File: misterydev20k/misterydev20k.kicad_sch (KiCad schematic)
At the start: 45 parts, among them J1 SWD, J2 USB_C_Receptacle_USB2.0, SW1 SW_Push, U1 XC6206PxxxMR-Regulator_Linear, U2 W25Q128JVS, U3 USBLC6-2SC6, U4 RP2040, Y1 12MHz

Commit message: Some dev board progress
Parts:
- added R51: 22, Resistor_SMD:R_0402_1005Metric, symbol Device:R_Small
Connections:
- net TCK: now also R51.2; no longer U4.18 (GPIO15)
- net ~{CFG}: now reaches U4.32 (GPIO21)
- net MODE0: now reaches U4.35 (GPIO23)
- net MODE1: now reaches U4.36 (GPIO24)
- new net: R51.1, U4.18 (GPIO15)
- no-connect marks 10 -> 7
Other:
- sheet GW2AR-LV18 FPGA ports: added MODE[0..1], ~{CFG}; removed none
- moved on the sheet: D1, R9

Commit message: More updates in dev20k
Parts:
- removed C4: 1uF, Capacitor_SMD:C_0402_1005Metric, symbol Device:C_Small
- removed FB5: MPZ1608S101, Inductor_SMD:L_0603_1608Metric, symbol Device:FerriteBead
- removed JP1: 3.3V, Jumper:SolderJumper-3_P1.3mm_Bridged12_RoundedPad1.0x1.5mm, symbol Jumper:SolderJumper_3_Bridged12
- removed R8: 1k, Resistor_SMD:R_0402_1005Metric, symbol Device:R_Small
- removed U1: XC6206PxxxMR-Regulator_Linear, Package_TO_SOT_SMD:SOT-23, symbol kicad-keyboard-parts:XC6206PxxxMR-Regulator_Linear
- added C37: 100nF, Capacitor_SMD:C_0402_1005Metric, symbol Device:C_Small
- added C38: 10uF, Capacitor_SMD:C_0402_1005Metric, symbol Device:C_Small
- added FB1: MPZ1608S101, Inductor_SMD:L_0603_1608Metric, symbol Device:FerriteBead
- added L1: 2.2uH, Inductor_SMD:L_0805_2012Metric, symbol Device:L
- added R36: 68k, Resistor_SMD:R_0402_1005Metric, symbol Device:R_Small
- added R37: 15k, Resistor_SMD:R_0402_1005Metric, symbol Device:R_Small
- added U10: TLV62569DBV, Package_TO_SOT_SMD:SOT-23-5, symbol Regulator_Switching:TLV62569DBV
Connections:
- net +3V3: now also FB1.2
- net +5V: now also C37.2, U10.1 (EN), U10.4 (VIN)
- net GND: now also C37.1, C38.1, R37.2, U10.2 (GND)
- new net: C38.2, FB1.1, L1.2, R36.1
- new net: R36.2, R37.1, U10.5 (FB)
- new net: L1.1, U10.3 (SW)
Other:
- sheet GW2AR-LV18 FPGA ports: added +3.3V; removed VCC33
- sheet USB Hub ports: added none; removed 12MHz
- note added: "or MT3520B"
- note removed: "RP2040 main 3.3V linear regulated power supply. Optionally replaced by the FPGAs switch mode 3.3V supply."
- moved on the sheet: C11, C12, C13, C14, C6, C7, C8

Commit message: dev20k update
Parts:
- removed C37: 100nF, Capacitor_SMD:C_0402_1005Metric, symbol Device:C_Small
- removed C38: 10uF, Capacitor_SMD:C_0402_1005Metric, symbol Device:C_Small
- removed FB1: MPZ1608S101, Inductor_SMD:L_0603_1608Metric, symbol Device:FerriteBead
- removed L1: 2.2uH, Inductor_SMD:L_0805_2012Metric, symbol Device:L
- removed R36: 68k, Resistor_SMD:R_0402_1005Metric, symbol Device:R_Small
- removed R37: 15k, Resistor_SMD:R_0402_1005Metric, symbol Device:R_Small
- removed U10: TLV62569DBV, Package_TO_SOT_SMD:SOT-23-5, symbol Regulator_Switching:TLV62569DBV
- added C51, C54: 100nF, Capacitor_SMD:C_0402_1005Metric, symbol Device:C_Small
- added C52, C57: 100nF, Capacitor_SMD:C_0603_1608Metric, symbol Device:C_Small
- added C53: 10uF, Capacitor_SMD:C_0603_1608Metric, symbol Device:C_Small
- added C55: 22pF, Capacitor_SMD:C_0402_1005Metric, symbol Device:C_Small
- added C56: 22uF, Capacitor_SMD:C_0603_1608Metric, symbol Device:C_Small
- added L3: 3.3uH, Inductor_SMD:L_Sunlord_MWSA0402S, symbol Device:L
- added R53: 47k, Resistor_SMD:R_0402_1005Metric, symbol Device:R_Small
- added R54, R55: 30k 1%, Resistor_SMD:R_0402_1005Metric, symbol Device:R_Small
- added R8: 30k, Resistor_SMD:R_0402_1005Metric, symbol Device:R_Small
- added U1: SY8113BADC, Package_TO_SOT_SMD:TSOT-23-6, symbol Regulator_Switching:LM2842Y
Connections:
- net +3V3: now also C55.2, C56.1, C57.1, L3.2, R54.2
- net +5V: now also C52.1, C53.1, R53.2, U1.5 (VIN)
- net GND: now also C51.1, C52.2, C53.2, C56.2, C57.2, R55.1, R8.1, U1.2 (GND)
- net ~{SD_DET}: now reaches U4.9 (GPIO7)
- net SD_CLK renamed SD_CLK_PI
- new net: C55.1, R54.1, R55.2, U1.3 (FB)
- new net: C54.1, U1.1 (BOOST)
- new net: C54.2, L3.1, U1.6 (SW)
- new net: C51.2, R53.1, R8.2, U1.4 (EN)
- no-connect marks 7 -> 6
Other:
- sheet GW2AR-LV18 FPGA ports: added SD_CLK_PI, ~{SD_DET}; removed SD_CLK
- note added: "TODO: Check Inductor!!!"
- note removed: "or MT3520B"

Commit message: Another board update
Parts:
- R54: value 30k 1% -> 15k 1%
- R55: value 30k 1% -> 3k3 1%
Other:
- note removed: "TODO: Check Inductor!!!"
- moved on the sheet: C55, C56, C57, L3, R54, R55

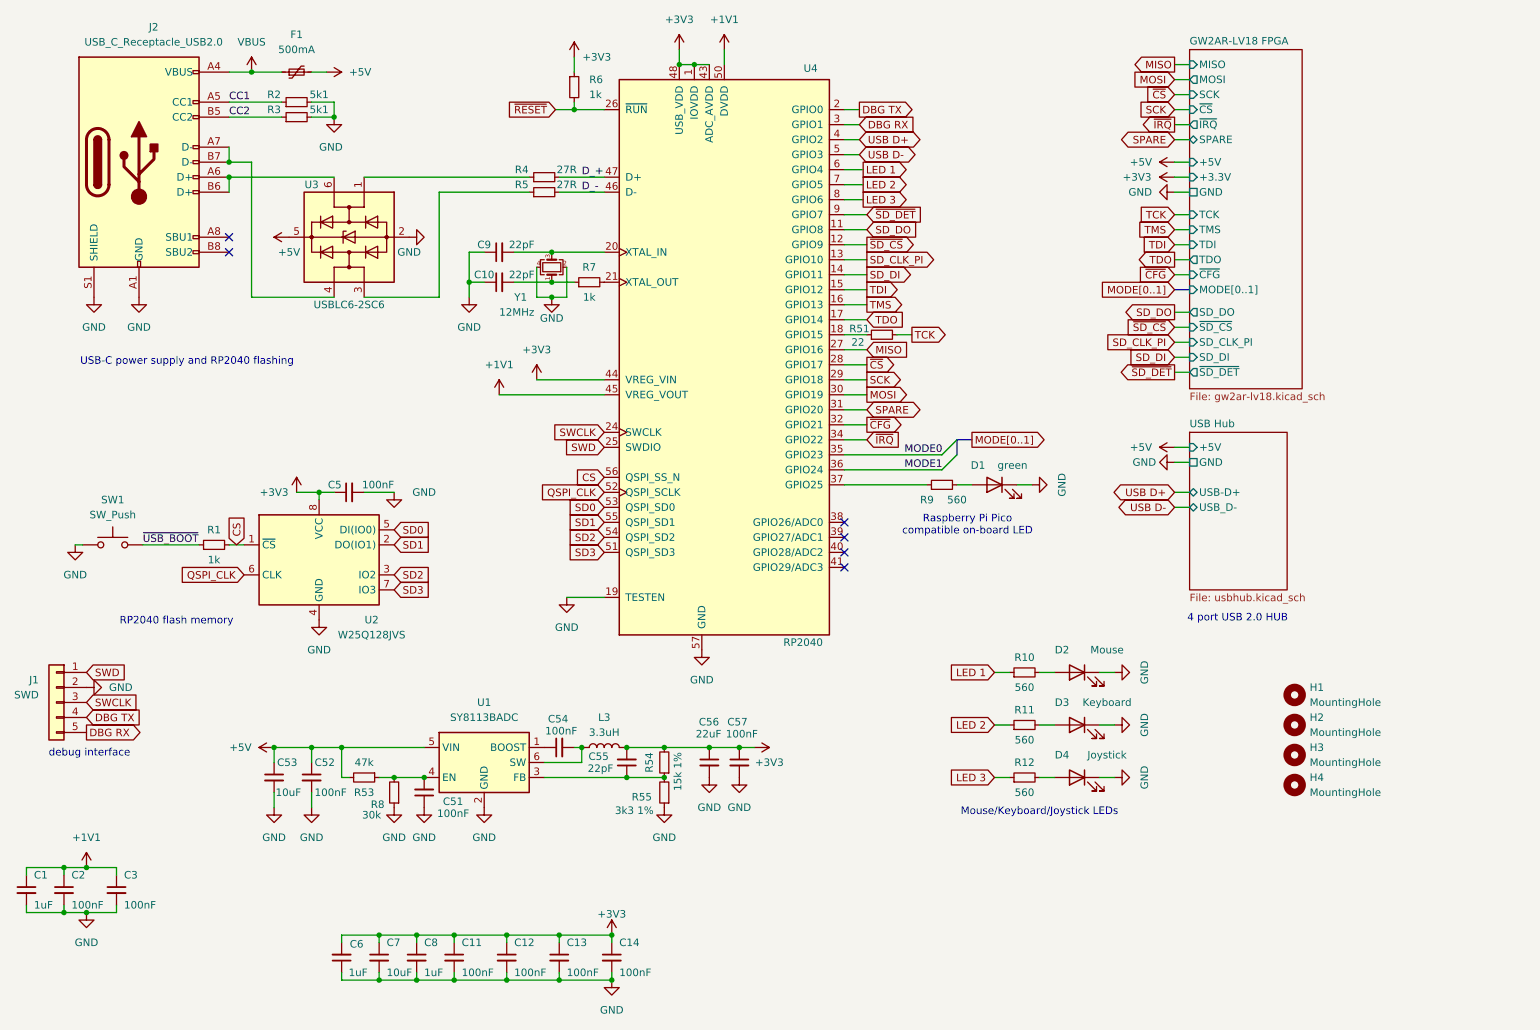
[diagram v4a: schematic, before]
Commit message: Fix dev20k schematic
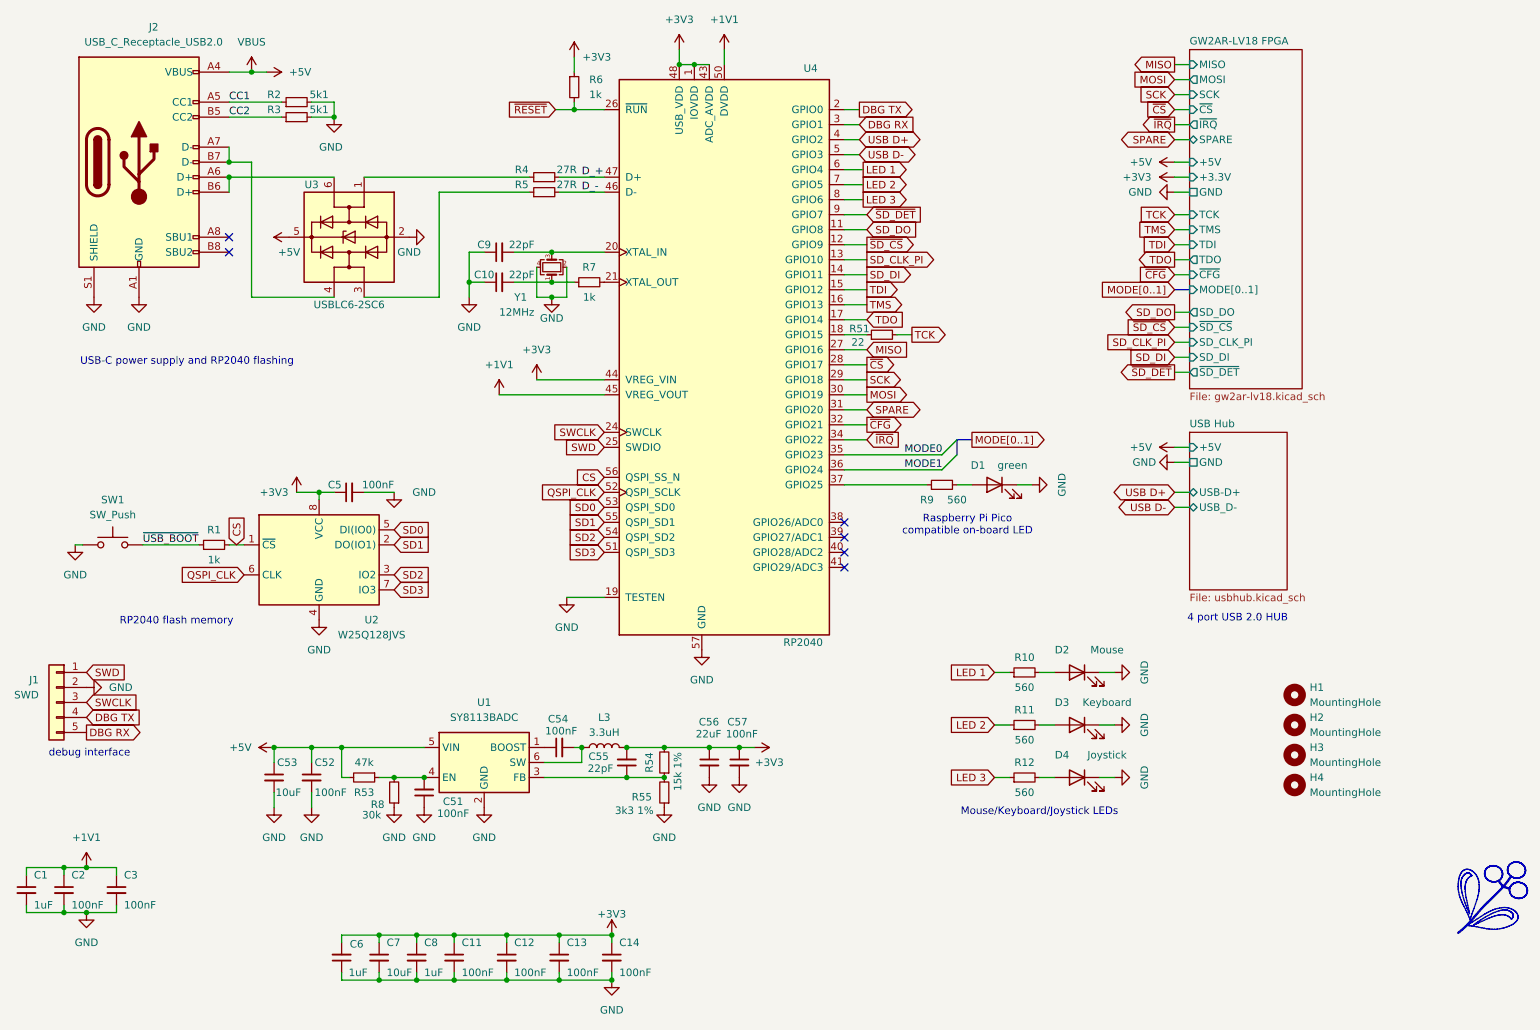
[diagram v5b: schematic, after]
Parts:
- removed F1: 500mA, Fuse:Fuse_1206_3216Metric, symbol Device:Polyfuse_Small
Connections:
- net VBUS is gone; now on net +5V: J2.A4 (VBUS), J2.A9 (VBUS), J2.B4 (VBUS), J2.B9 (VBUS)
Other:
- title: MiSTery 20k Development Board -> MiSTeryDev 20k - FPGA Companion MCU

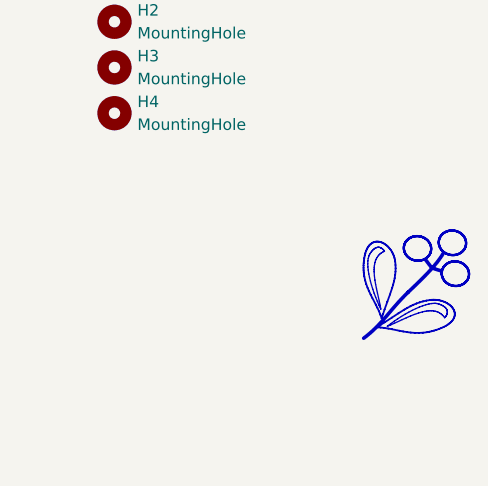
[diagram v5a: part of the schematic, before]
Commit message: Update pin table
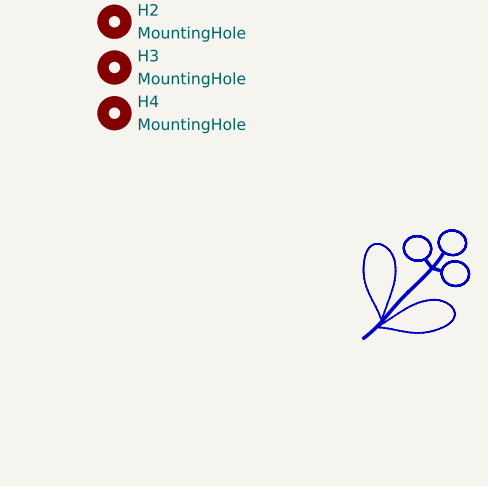
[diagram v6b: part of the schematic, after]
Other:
- title: MiSTeryDev 20k - FPGA Companion MCU -> MiSTle - MiSTeryDev20k
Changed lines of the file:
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@@
 	(paper "A4")
 	(title_block
-		(title "MiSTeryDev 20k - FPGA Companion MCU")
+		(title "MiSTle - MiSTeryDev20k")
 		(date "2025-08-28")
 		(rev "1.0")
 		(company "Till Harbaum")
-	)
-	(polyline
-		(pts
-			(xy 279.5138 176.0698) (xy 279.6412 176.0823) (xy 279.7608 176.1043) (xy 279.8723 176.1363) (xy 279.9762 176.174)
-			(xy 280.0733 176.2131) (xy 280.164 176.2535) (xy 280.2482 176.2952) (xy 280.3261 176.3381) (xy 280.3978 176.3821)
-			(xy 280.4635 176.4271) (xy 280.5234 176.4731) (xy 280.5774 176.52) (xy 280.6258 176.5676) (xy 280.6687 176.616)
-			(xy 280.7062 176.6651) (xy 280.7384 176.7148) (xy 280.7655 176.7649) (xy 280.7877 176.8155) (xy 280.8049 176.8664)
-			(xy 280.8175 176.9177) (xy 280.8254 176.9691) (xy 280.8289 177.0206) (xy 280.828 177.0722) (xy 280.8229 177.1238)
-			(xy 280.8137 177.1753) (xy 280.8006 177.2266) (xy 280.7836 177.2777) (xy 280.763 177.3284) (xy 280.7388 177.3787)
-			(xy 280.7112 177.4286) (xy 280.6802 177.4779) (xy 280.6461 177.5266) (xy 280.609 177.5746) (xy 280.5689 177.6218)
-			(xy 280.5261 177.6682) (xy 280.4018 177.5021) (xy 280.2674 177.3583) (xy 280.1235 177.2358) (xy 279.9705 177.1336)
-			(xy 279.8089 177.0507) (xy 279.6394 176.9862) (xy 279.4624 176.9392) (xy 279.2784 176.9086) (xy 279.0881 176.8935)
-			(xy 278.8919 176.8929) (xy 278.6903 176.906) (xy 278.4838 176.9317) (xy 278.2731 176.969) (xy 278.0586 177.017)
-			(xy 277.6204 177.1414) (xy 277.1734 177.2971) (xy 276.7219 177.4764) (xy 276.2701 177.6716) (xy 275.8221 177.8751)
-			(xy 274.9549 178.276) (xy 274.544 178.4582) (xy 274.1539 178.6178) (xy 274.5308 178.3322) (xy 274.9192 178.0535)
-			(xy 275.3163 177.784) (xy 275.719 177.5259) (xy 276.1241 177.2814) (xy 276.5287 177.0529) (xy 276.9297 176.8425)
-			(xy 277.324 176.6525) (xy 277.7086 176.4851) (xy 278.0805 176.3427) (xy 278.4365 176.2274) (xy 278.7736 176.1414)
-			(xy 279.0888 176.0871) (xy 279.379 176.0666) (xy 279.5138 176.0698)
-		)
-		(stroke
-			(width -0.0001)
-			(type solid)
-		)
-		(fill
-			(type color)
-			(color 30 188 94 1)
-		)
+		(comment 1 "FPGA Companion MCU")
 	)
 	(bezier
@@
 			(width 0.4)
 			(type solid)
+			(color 0 0 0 1)
 		)
 		(fill
@@
 		)
 	)
-	(polyline
-		(pts
-			(xy 273.2247 169.8384) (xy 273.2758 169.8459) (xy 273.3261 169.8576) (xy 273.3754 169.8734) (xy 273.4238 169.8932)
-			(xy 273.4712 169.9169) (xy 273.5176 169.9442) (xy 273.5628 169.975) (xy 273.607 170.0093) (xy 273.6499 170.0468)
-			(xy 273.6916 170.0874) (xy 273.732 170.131) (xy 273.7711 170.1774) (xy 273.8089 170.2265) (xy 273.8452 170.2781)
-			(xy 273.6567 170.3647) (xy 273.4879 170.4658) (xy 273.3378 170.5808) (xy 273.2057 170.7089) (xy 273.0907 170.8494)
-			(xy 272.992 171.0015) (xy 272.9088 171.1647) (xy 272.8402 171.3381) (xy 272.7854 171.521) (xy 272.7436 171.7127)
-			(xy 272.714 171.9126) (xy 272.6957 172.1198) (xy 272.6879 172.3337) (xy 272.6897 172.5535) (xy 272.7192 173.008)
-			(xy 272.7774 173.4778) (xy 272.8577 173.9569) (xy 272.9535 174.4397) (xy 273.0583 174.9204) (xy 273.2679 175.8525)
-			(xy 273.3596 176.2925) (xy 273.4336 176.7075) (xy 273.2336 176.279) (xy 273.0428 175.8406) (xy 272.8628 175.3957)
-			(xy 272.6952 174.9478) (xy 272.5414 174.5003) (xy 272.403 174.0567) (xy 272.2817 173.6204) (xy 272.1789 173.1949)
-			(xy 272.0961 172.7837) (xy 272.0351 172.3903) (xy 271.9972 172.018) (xy 271.984 171.6703) (xy 271.9972 171.3507)
-			(xy 272.0382 171.0627) (xy 272.1087 170.8097) (xy 272.1554 170.6974) (xy 272.21 170.5951) (xy 272.2687 170.5015)
-			(xy 272.3274 170.4147) (xy 272.386 170.3346) (xy 272.4445 170.2611) (xy 272.5028 170.1939) (xy 272.5609 170.133)
-			(xy 272.6187 170.0782) (xy 272.6763 170.0294) (xy 272.7335 169.9865) (xy 272.7902 169.9492) (xy 272.8466 169.9174)
-			(xy 272.9024 169.8911) (xy 272.9578 169.87) (xy 273.0125 169.854) (xy 273.0666 169.843) (xy 273.12 169.8369)
-			(xy 273.1727 169.8354) (xy 273.2247 169.8384)
-		)
-		(stroke
-			(width -0.0001)
-			(type solid)
-		)
-		(fill
-			(type color)
-			(color 30 188 94 1)
-		)
-	)
 	(bezier
 		(pts
@@
 			(width 0.4)
 			(type solid)
+			(color 0 0 0 1)
 		)
 		(fill
@@
 			(width 0.2)
 			(type solid)
+			(color 0 0 0 1)
 		)
 		(fill
@@
 	(polyline
 		(pts
-			(xy 273.2477 169.2225) (xy 273.3911 169.2549) (xy 273.5339 169.3026) (xy 273.6752 169.365) (xy 273.8142 169.4415)
-			(xy 273.95 169.5313) (xy 274.0819 169.6339) (xy 274.2089 169.7484) (xy 274.3302 169.8744) (xy 274.4451 170.011)
-			(xy 274.5525 170.1577) (xy 274.6518 170.3138) (xy 274.742 170.4786) (xy 274.8223 170.6514) (xy 274.8918 170.8316)
-			(xy 274.9498 171.0185) (xy 274.9954 171.2115) (xy 275.0277 171.4099) (xy 275.0648 171.8037) (xy 275.0758 172.1837)
-			(xy 275.0626 172.5529) (xy 275.027 172.9144) (xy 274.9709 173.2712) (xy 274.8961 173.6262) (xy 274.8044 173.9824)
-			(xy 274.6978 174.3429) (xy 274.4468 175.0887) (xy 274.158 175.8875) (xy 273.8461 176.7634) (xy 273.6861 177.2377)
-			(xy 273.5259 177.7403) (xy 273.3867 177.3352) (xy 273.2277 176.9454) (xy 273.0536 176.5673) (xy 272.8692 176.1971)
-			(xy 272.4888 175.4658) (xy 272.3023 175.0973) (xy 272.1246 174.7221) (xy 271.9605 174.3364) (xy 271.8149 173.9365)
-			(xy 271.6925 173.5187) (xy 271.598 173.0794) (xy 271.5628 172.8506) (xy 271.5364 172.6149) (xy 271.5193 172.3721)
-			(xy 271.5122 172.1215) (xy 271.5157 171.8628) (xy 271.5304 171.5955) (xy 271.5569 171.3191) (xy 271.5957 171.0332)
-			(xy 271.6473 170.7553) (xy 271.7108 170.5027) (xy 271.7855 170.2747) (xy 271.8706 170.0708) (xy 271.9652 169.8903)
-			(xy 272.0684 169.7324) (xy 272.1794 169.5966) (xy 272.2974 169.4821) (xy 272.4216 169.3882) (xy 272.551 169.3144)
-			(xy 272.6848 169.26) (xy 272.8223 169.2243) (xy 272.9625 169.2065) (xy 273.1046 169.2062) (xy 273.2477 169.2225)
+			(xy 273.2477 169.4765) (xy 273.3911 169.5089) (xy 273.5339 169.5566) (xy 273.6752 169.619) (xy 273.8142 169.6955)
+			(xy 273.95 169.7853) (xy 274.0819 169.8879) (xy 274.2089 170.0024) (xy 274.3302 170.1284) (xy 274.4451 170.265)
+			(xy 274.5525 170.4117) (xy 274.6518 170.5678) (xy 274.742 170.7326) (xy 274.8223 170.9054) (xy 274.8918 171.0856)
+			(xy 274.9498 171.2725) (xy 274.9954 171.4655) (xy 275.0277 171.6639) (xy 275.0648 172.0577) (xy 275.0758 172.4377)
+			(xy 275.0626 172.8069) (xy 275.027 173.1684) (xy 274.9709 173.5252) (xy 274.8961 173.8802) (xy 274.8044 174.2364)
+			(xy 274.6978 174.5969) (xy 274.4468 175.3427) (xy 274.158 176.1415) (xy 273.8461 177.0174) (xy 273.6861 177.4917)
+			(xy 273.5259 177.9943) (xy 273.3867 177.5892) (xy 273.2277 177.1994) (xy 273.0536 176.8213) (xy 272.8692 176.4511)
+			(xy 272.4888 175.7198) (xy 272.3023 175.3513) (xy 272.1246 174.9761) (xy 271.9605 174.5904) (xy 271.8149 174.1905)
+			(xy 271.6925 173.7727) (xy 271.598 173.3334) (xy 271.5628 173.1046) (xy 271.5364 172.8689) (xy 271.5193 172.6261)
+			(xy 271.5122 172.3755) (xy 271.5157 172.1168) (xy 271.5304 171.8495) (xy 271.5569 171.5731) (xy 271.5957 171.2872)
+			(xy 271.6473 171.0093) (xy 271.7108 170.7567) (xy 271.7855 170.5287) (xy 271.8706 170.3248) (xy 271.9652 170.1443)
+			(xy 272.0684 169.9864) (xy 272.1794 169.8506) (xy 272.2974 169.7361) (xy 272.4216 169.6422) (xy 272.551 169.5684)
+			(xy 272.6848 169.514) (xy 272.8223 169.4783) (xy 272.9625 169.4605) (xy 273.1046 169.4602) (xy 273.2477 169.4765)
 		)
 		(stroke
 			(width 0.2)
 			(type solid)
+			(color 0 0 0 1)
 		)
 		(fill
@@
 			(width 0.2593)
 			(type solid)
+			(color 0 0 0 1)
 		)
 		(fill
 			(type color)
-			(color 255 255 255 1)
+			(color 194 194 194 1)
 		)
 	)
@@
 			(width 0.2593)
 			(type solid)
+			(color 0 0 0 1)
 		)
 		(fill
 			(type color)
-			(color 255 255 255 1)
+			(color 194 194 194 1)
 		)
 	)
@@
 			(width 0.2593)
 			(type solid)
+			(color 0 0 0 1)
 		)
 		(fill
 			(type color)
-			(color 255 255 255 1)
+			(color 194 194 194 1)
 		)
 	)
@@
 			(width 0.4)
 			(type solid)
+			(color 0 0 0 1)
 		)
 	)
@@
 			(width 0.4)
 			(type solid)
-		)
-	)
+			(color 0 0 0 1)
+		)
+	)

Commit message: Further work on the dev20k
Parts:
- added JP1: SRC D+, Jumper:SolderJumper-3_P1.3mm_Bridged12_RoundedPad1.0x1.5mm, symbol Jumper:SolderJumper_3_Bridged12
- added JP2: SRC D-, Jumper:SolderJumper-3_P1.3mm_Bridged12_RoundedPad1.0x1.5mm, symbol Jumper:SolderJumper_3_Bridged12
- SW1: value SW_Push -> Boot
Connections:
- net USB D+: now also JP1.3 (B)
- net USB D-: now also JP2.3 (B)
- net at U3.1 (I/O1): now also JP1.1 (A); no longer R4.1
- net at U3.3 (I/O2): now also JP2.1 (A); no longer R5.1
- net CS: no longer names the net of R1.2, U2.1 (~{CS}), U4.56 (QSPI_SS_N)
- net QSPI_CLK: no longer names the net of U2.6 (CLK), U4.52 (QSPI_SCLK)
- net SD0: no longer names the net of U2.5 (DI(IO0)), U4.53 (QSPI_SD0)
- net SD1: no longer names the net of U2.2 (DO(IO1)), U4.55 (QSPI_SD1)
- net SD2: no longer names the net of U2.3 (IO2), U4.54 (QSPI_SD2)
- net SD3: no longer names the net of U2.7 (IO3), U4.51 (QSPI_SD3)
- new net: JP2.2 (C), R5.1
- new net: JP1.2 (C), R4.1
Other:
- note added: "USB-C power supply and RP2040 flashing Jumper option to reroute to USB Hub"
- note removed: "USB-C power supply and RP2040 flashing"
- moved on the sheet: C5, R1, R4, R5, SW1, U2

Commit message: Update mon tx/rx and spare 5 pins
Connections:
- net SPARE: no longer names the net of U4.31 (GPIO20)
- no-connect marks 6 -> 7
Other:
- sheet GW2AR-LV18 FPGA ports: added MON_RX, MON_TX; removed SPARE
- sheet USB Hub ports: added USB_D+; removed USB-D+
